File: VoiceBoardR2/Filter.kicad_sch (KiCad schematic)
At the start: 32 parts, among them Q301 BC858, Q302 BC858, U301 TL074, U303 LM13700, U304 MCP4018-103E/LT

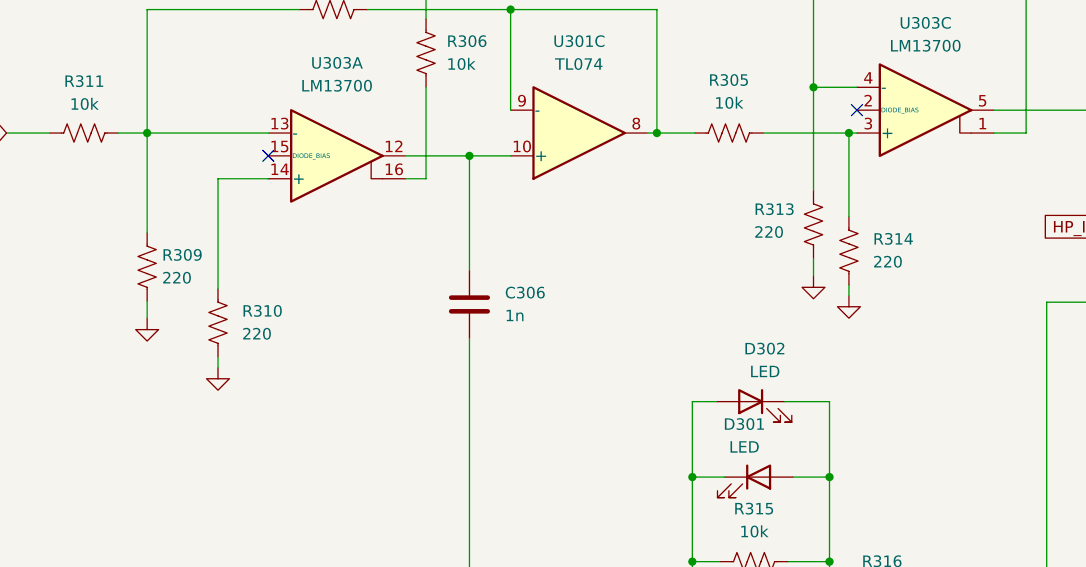
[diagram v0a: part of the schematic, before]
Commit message: filter simulation
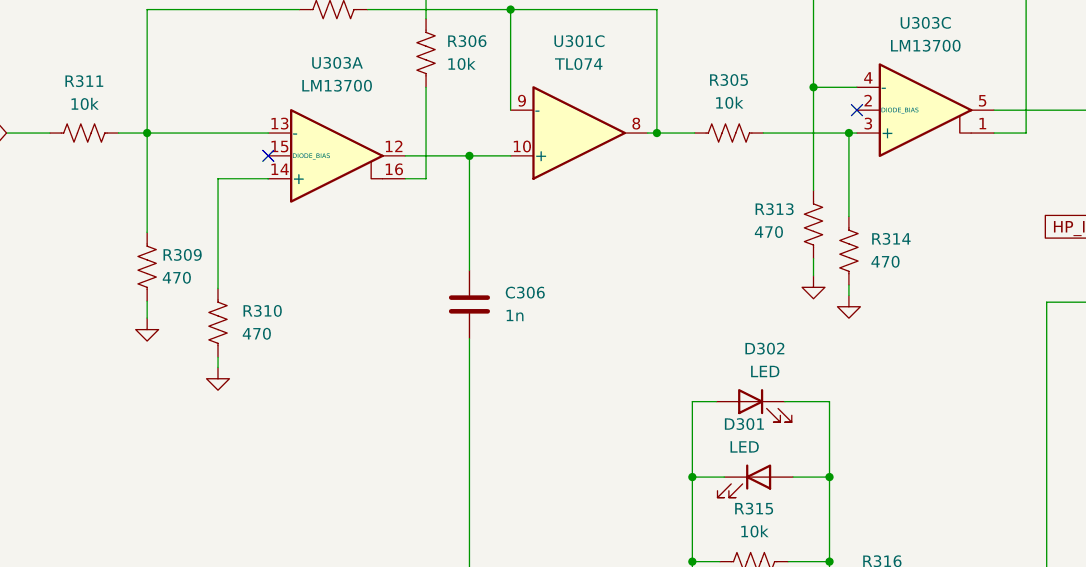
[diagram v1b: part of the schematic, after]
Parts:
- R309, R310, R313, R314: value 220 -> 470
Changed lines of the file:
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@@
       (effects (font (size 1.27 1.27)) (justify right))
     )
-    (property "Value" "220" (at 74.93 119.126 0)
+    (property "Value" "470" (at 74.93 119.126 0)
       (effects (font (size 1.27 1.27)) (justify right))
     )
@@
       (effects (font (size 1.27 1.27)) (justify right))
     )
-    (property "Value" "220" (at 66.04 112.903 0)
+    (property "Value" "470" (at 66.04 112.903 0)
       (effects (font (size 1.27 1.27)) (justify right))
     )
@@
       (effects (font (size 1.27 1.27)) (justify right))
     )
-    (property "Value" "220" (at 131.826 107.823 0)
+    (property "Value" "470" (at 131.826 107.823 0)
       (effects (font (size 1.27 1.27)) (justify right))
     )
@@
   (symbol (lib_id "Device:R_US") (at 142.367 109.855 180) (unit 1)
     (in_bom yes) (on_board yes) (dnp no) (fields_autoplaced)
-    (property "Reference" "R314" (at 145.034 108.585 0)
+    (property "Reference" "R314" (at 144.78 108.585 0)
       (effects (font (size 1.27 1.27)) (justify right))
     )
-    (property "Value" "220" (at 145.034 111.125 0)
+    (property "Value" "470" (at 144.78 111.125 0)
       (effects (font (size 1.27 1.27)) (justify right))
     )
